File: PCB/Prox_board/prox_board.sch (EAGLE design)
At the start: 7 parts

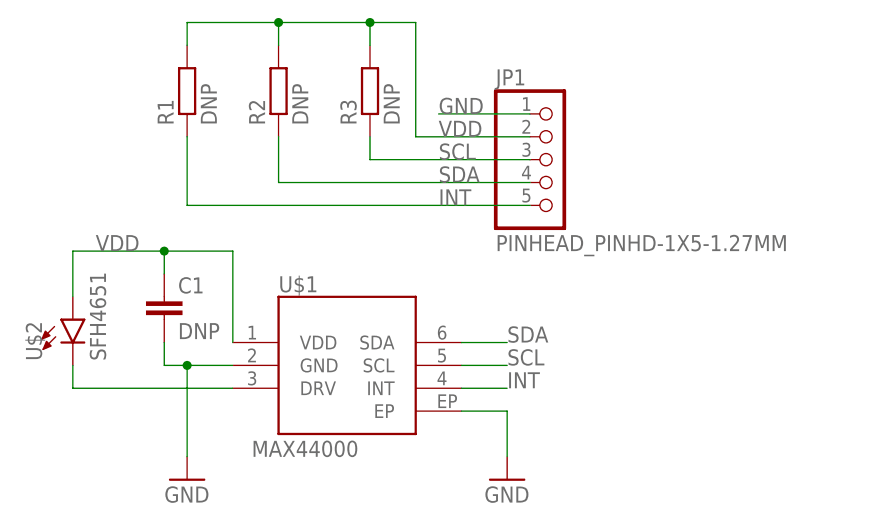
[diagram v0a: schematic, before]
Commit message: Created board file for proximity
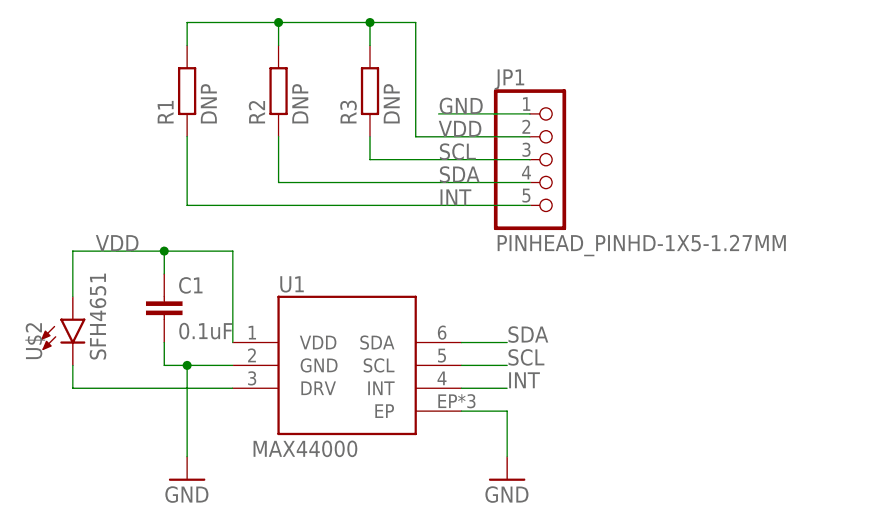
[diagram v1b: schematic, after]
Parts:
- removed U$1: MAX44000, robot_pcb2:MAX44000
- added U1: MAX44000, Wisp5_Harvester_Motor-driver_V2:MAX44000
- C1: value DNP -> 0.1uF
- JP1: device Wisp5_Harvester_Motor-driver:PINHEAD_PINHD-1X5-1.27MM -> Wisp5_Harvester_Motor-driver_V2:PINHEAD_PINHD-1X5-1.27MM
- U$2: device robot_pcb2:SFH4651 -> Wisp5_Harvester_Motor-driver_V2:SFH4651
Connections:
- net GND: now also U1.EP, U1.GND; no longer U$1.EP, U$1.GND
- net INT: now also U1.INT; no longer U$1.INT
- net N$1: now also U1.DRV; no longer U$1.DRV
- net SCL: now also U1.SCL; no longer U$1.SCL
- net SDA: now also U1.SDA; no longer U$1.SDA
- net VDD: now also U1.VDD; no longer U$1.VDD
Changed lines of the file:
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@@
 <?xml version="1.0" encoding="utf-8"?>
 <!DOCTYPE eagle SYSTEM "eagle.dtd">
-<eagle version="8.2.1">
+<eagle version="8.2.2">
 <drawing>
 <settings>
@@
 </classes>
 <parts>
-<part name="U$1" library="robot_pcb2" deviceset="MAX44000" device=""/>
-<part name="U$2" library="robot_pcb2" deviceset="SFH4651" device=""/>
-<part name="JP1" library="Wisp5_Harvester_Motor-driver" deviceset="PINHEAD_PINHD-1X5-1.27MM" device=""/>
+<part name="U1" library="Wisp5_Harvester_Motor-driver_V2" deviceset="MAX44000" device=""/>
+<part name="U$2" library="Wisp5_Harvester_Motor-driver_V2" deviceset="SFH4651" device=""/>
+<part name="JP1" library="Wisp5_Harvester_Motor-driver_V2" deviceset="PINHEAD_PINHD-1X5-1.27MM" device=""/>
 <part name="GND1" library="Wisp5_Harvester_Motor-driver" deviceset="GND" device=""/>
 <part name="GND2" library="Wisp5_Harvester_Motor-driver" deviceset="GND" device=""/>
@@
 <part name="R2" library="resistor" deviceset="R-EU_" device="R0603" value="DNP"/>
 <part name="R3" library="resistor" deviceset="R-EU_" device="R0603" value="DNP"/>
-<part name="C1" library="resistor" deviceset="C-EU" device="C0603" value="DNP"/>
+<part name="C1" library="resistor" deviceset="C-EU" device="C0603" value="0.1uF"/>
 </parts>
 <sheets>
@@
 </plain>
 <instances>
-<instance part="U$1" gate="G$1" x="35.56" y="17.78"/>
+<instance part="U1" gate="G$1" x="35.56" y="17.78"/>
 <instance part="U$2" gate="G$1" x="5.08" y="22.86"/>
 <instance part="JP1" gate="G$1" x="58.42" y="40.64"/>
@@
 <pinref part="GND1" gate="1" pin="GND"/>
 <wire x1="17.78" y1="7.62" x2="17.78" y2="17.78" width="0.1524" layer="91"/>
-<pinref part="U$1" gate="G$1" pin="GND"/>
+<pinref part="U1" gate="G$1" pin="GND"/>
 <wire x1="17.78" y1="17.78" x2="22.86" y2="17.78" width="0.1524" layer="91"/>
 <pinref part="C1" gate="G$1" pin="2"/>
@@
 <pinref part="GND2" gate="1" pin="GND"/>
 <wire x1="53.34" y1="7.62" x2="53.34" y2="12.7" width="0.1524" layer="91"/>
-<pinref part="U$1" gate="G$1" pin="EP"/>
+<pinref part="U1" gate="G$1" pin="EP"/>
 <wire x1="53.34" y1="12.7" x2="48.26" y2="12.7" width="0.1524" layer="91"/>
 </segment>
@@
 <pinref part="U$2" gate="G$1" pin="C"/>
 <wire x1="5.08" y1="17.78" x2="5.08" y2="15.24" width="0.1524" layer="91"/>
-<pinref part="U$1" gate="G$1" pin="DRV"/>
+<pinref part="U1" gate="G$1" pin="DRV"/>
 <wire x1="5.08" y1="15.24" x2="22.86" y2="15.24" width="0.1524" layer="91"/>
 </segment>
@@
 <net name="SDA" class="0">
 <segment>
-<pinref part="U$1" gate="G$1" pin="SDA"/>
+<pinref part="U1" gate="G$1" pin="SDA"/>
 <wire x1="48.26" y1="20.32" x2="53.34" y2="20.32" width="0.1524" layer="91"/>
 <label x="53.34" y="20.32" size="1.778" layer="95"/>
@@
 <net name="SCL" class="0">
 <segment>
-<pinref part="U$1" gate="G$1" pin="SCL"/>
+<pinref part="U1" gate="G$1" pin="SCL"/>
 <wire x1="48.26" y1="17.78" x2="53.34" y2="17.78" width="0.1524" layer="91"/>
 <label x="53.34" y="17.78" size="1.778" layer="95"/>
@@
 <net name="INT" class="0">
 <segment>
-<pinref part="U$1" gate="G$1" pin="INT"/>
+<pinref part="U1" gate="G$1" pin="INT"/>
 <wire x1="48.26" y1="15.24" x2="53.34" y2="15.24" width="0.1524" layer="91"/>
 <label x="53.34" y="15.24" size="1.778" layer="95"/>
@@
 </segment>
 <segment>
-<pinref part="U$1" gate="G$1" pin="VDD"/>
+<pinref part="U1" gate="G$1" pin="VDD"/>
 <wire x1="22.86" y1="30.48" x2="22.86" y2="20.32" width="0.1524" layer="91"/>
 <pinref part="C1" gate="G$1" pin="1"/>
